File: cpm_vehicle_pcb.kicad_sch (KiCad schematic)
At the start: 71 parts, among them IC1 ATMEGAAU, IC2 RPI-ZERO, J1 Conn_02x03_Counter_Clockwise, J2 Conn_02x03_Counter_Clockwise, J3 Conn_01x05, J5 USB_B_Mini, J6 Conn_01x03_Socket, P1 NCP1117, Q11 BSS123, Q12 BSS123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

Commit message: Some Routing
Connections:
- net ERW1: now also EXT_PINS0.4, IC1.74 ((AD4)PA4); no longer EXT_PINS0.3, IC1.71 ((AD7)PA7)
- net ERW2: now also EXT_PINS0.6, IC1.73 ((AD5)PA5); no longer EXT_PINS0.5, IC1.72 ((AD6)PA6)
- net ERW3: now also EXT_PINS0.8, IC1.72 ((AD6)PA6); no longer EXT_PINS0.7, IC1.73 ((AD5)PA5)
- net ERW4: now also EXT_PINS0.10, IC1.71 ((AD7)PA7); no longer EXT_PINS0.9, IC1.74 ((AD4)PA4)
- net ERW5: now also EXT_PINS0.3; no longer EXT_PINS0.4
- net ERW6: now also EXT_PINS0.5, IC1.7 ((OC3C/INT5)PE5); no longer EXT_PINS0.6, IC1.16 (PH4(OC4B))
- net ERW7: now also EXT_PINS0.7, IC1.6 ((OC3B/INT4)PE4); no longer EXT_PINS0.8, IC1.24 ((OC1A/PCINT5)PB5)
- net ERW8: now also EXT_PINS0.9, IC1.5 ((OC3A/AIN1)PE3); no longer EXT_PINS0.10, IC1.23 ((OC2A/PCINT4)PB4)
- net GND: now also J2.5 (Pin_5); no longer J2.6 (Pin_6)
- net LED1: now also IC1.23 ((OC2A/PCINT4)PB4); no longer IC1.26 ((OC0A/OC1C/PCINT7)PB7)
- net LED2: now also IC1.16 (PH4(OC4B)); no longer IC1.27 (PH7(T4))
- net LED3: now also IC1.17 (PH5(OC4C)); no longer IC1.18 (PH6(OC2B))
- net LED4: now also IC1.18 (PH6(OC2B)); no longer IC1.17 (PH5(OC4C))
- net LED_BUILT_IN: now also IC1.26 ((OC0A/OC1C/PCINT7)PB7); no longer IC1.25 ((OC1B/PCINT6)PB6)
- net PWM: now also IC1.25 ((OC1B/PCINT6)PB6); no longer IC1.8 ((T3/INT6)PE6)
- net RX0: now also IC1.2 ((RXD0/PCIN8)PE0); no longer IC1.4 ((XCK0/AIN0)PE2)
- net SENSOR1: now also J2.6 (Pin_6); no longer J2.3 (Pin_3)
- net SENSOR2: now also J2.4 (Pin_4); no longer J2.5 (Pin_5)
- net SERVO_PWM: now also IC1.24 ((OC1A/PCINT5)PB5); no longer IC1.7 ((OC3C/INT5)PE5)
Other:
- moved on the sheet: C71, QG1

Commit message: update
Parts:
- added J4: USB4105-GF-A, footprints_vehicle_pcb:GCT_USB4105-GF-A, symbol USBC:USB4105-GF-A
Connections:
- net GND: now also J4.A1_B12 (GND), J4.B1_A12 (GND)
- net at C7.2, L1.1, U4.4 (EN)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: now also J4.A4_B9 (VBUS), J4.B4_A9 (VBUS)
- new net: J4.SH1 (SHELL_GND), J4.SH2 (SHELL_GND), J4.SH3 (SHELL_GND), J4.SH4 (SHELL_GND)
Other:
- moved on the sheet: C3, C4, C7, D1, D6, L1, R21, RV1, U4

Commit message: Routing 2
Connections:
- net LED1_PIN: now also J1.5 (Pin_5); no longer J1.3 (Pin_3)
- net LED2_PIN: now also J1.3 (Pin_3); no longer J1.4 (Pin_4)
- net LED4_PIN: now also J1.4 (Pin_4); no longer J1.5 (Pin_5)
- net PWM: now also J3.1 (Pin_1); no longer J3.5 (Pin_5)
- net SERVO_PWM: now also J3.5 (Pin_5); no longer J3.1 (Pin_1)
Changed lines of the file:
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@@
 		)
 	)
-	(label "LED2_PIN"
+	(label "LED4_PIN"
 		(at 66.04 231.14 0)
 		(effects
@@
 		)
 	)
-	(label "SERVO_PWM"
+	(label "PWM"
 		(at 55.88 255.27 0)
 		(effects
@@
 		)
 	)
-	(label "LED1_PIN"
+	(label "LED2_PIN"
 		(at 38.1 231.14 0)
 		(effects
@@
 		)
 	)
-	(label "PWM"
+	(label "SERVO_PWM"
 		(at 59.69 265.43 0)
 		(effects
@@
 		)
 	)
-	(label "LED4_PIN"
+	(label "LED1_PIN"
 		(at 66.04 228.6 0)
 		(effects

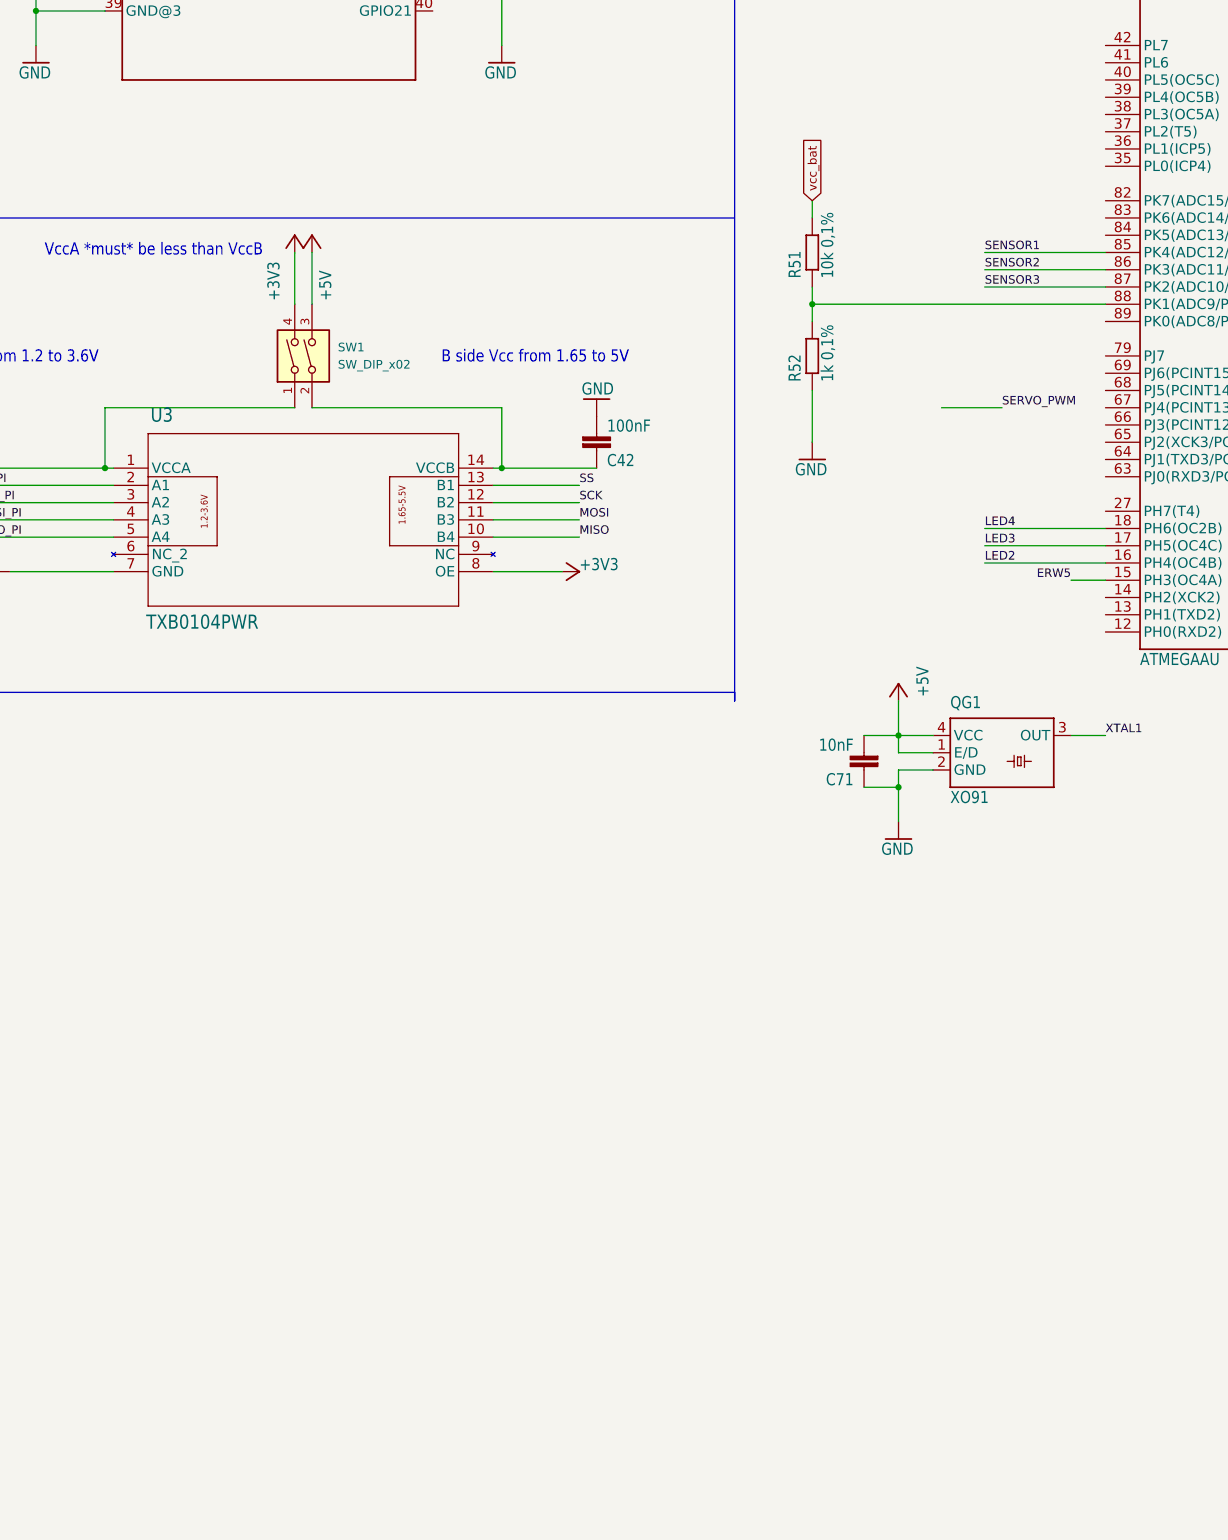
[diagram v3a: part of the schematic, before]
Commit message: Added Bq25887
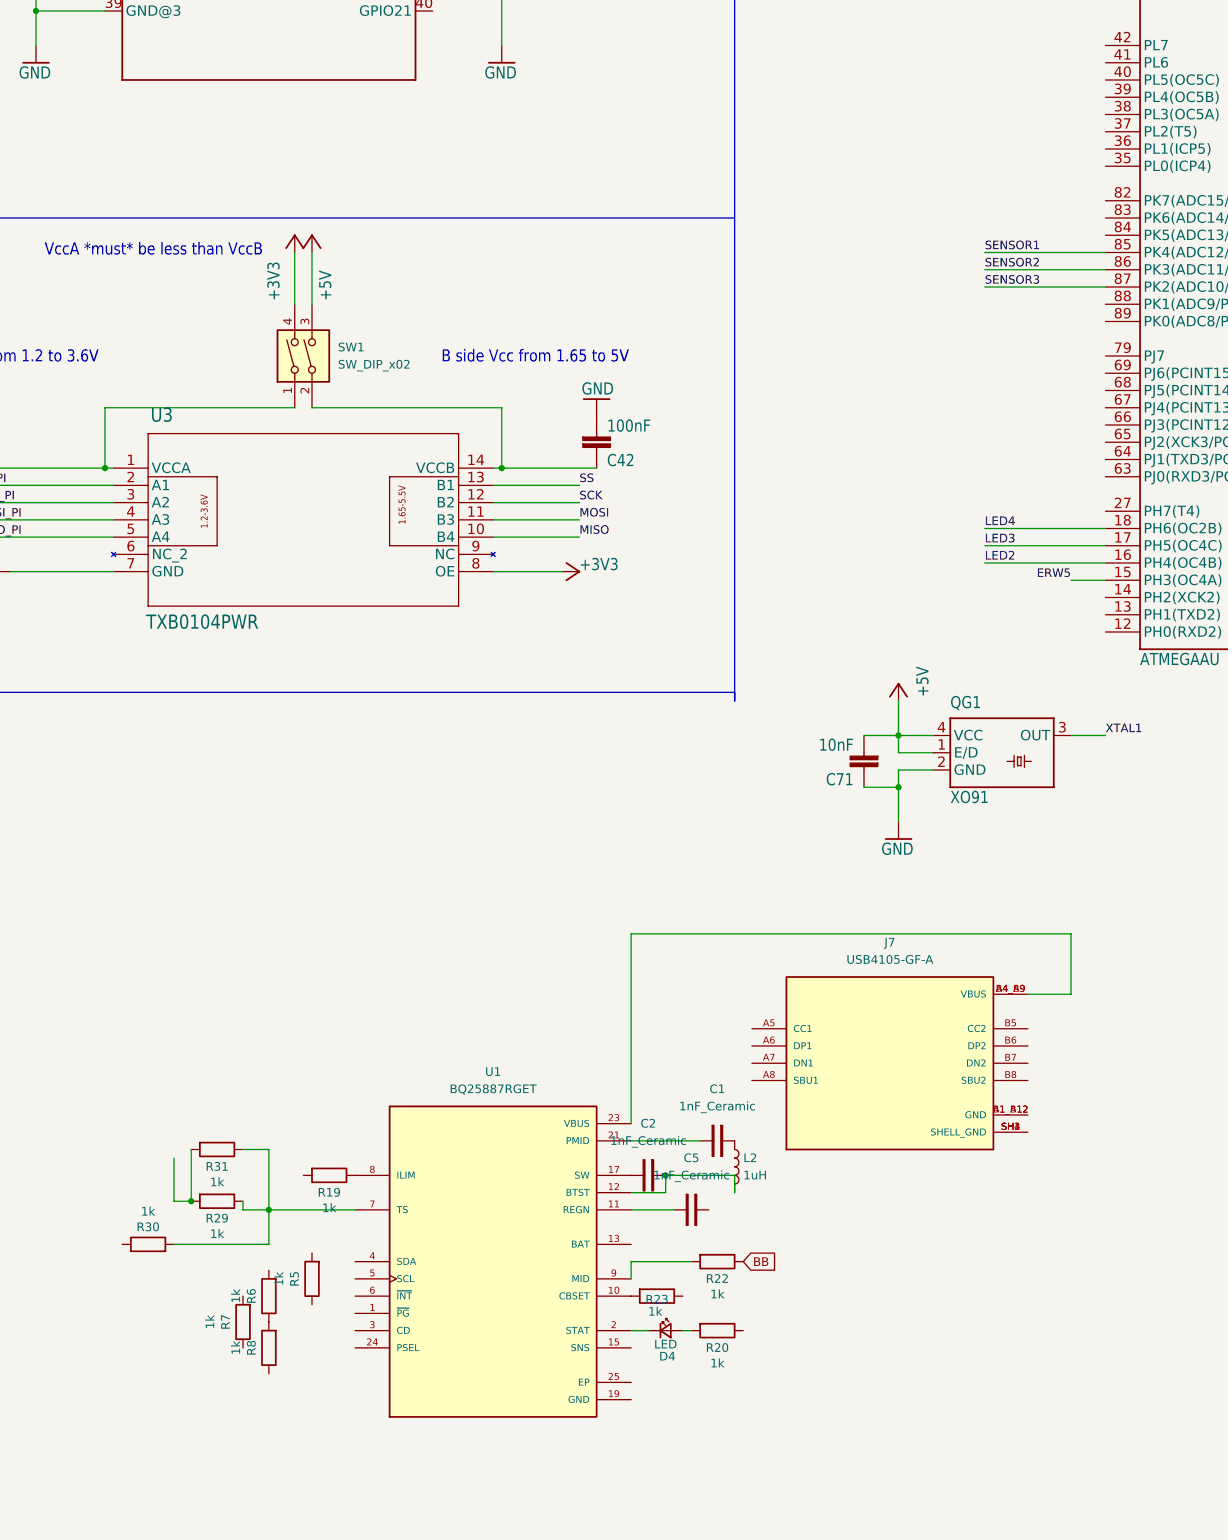
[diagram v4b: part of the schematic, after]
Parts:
- removed R51: 10k 0,1%, Resistor_SMD:R_0603_1608Metric, symbol main_board_V2.4-eagle-import:embedded_10681391_R-EUR0805
- removed R52: 1k 0,1%, Resistor_SMD:R_0603_1608Metric, symbol main_board_V2.4-eagle-import:embedded_10681391_R-EUR0805
- added C1, C2, C5: 1nF_Ceramic, Capacitor_THT:C_Disc_D5.0mm_W2.5mm_P2.50mm, symbol PCM_SL_Capacitors:1nF_Ceramic
- added D4: LED, PCM_SparkFun-LED:LED_0603_1608Metric, symbol PCM_SparkFun-LED:LED
- added J7: USB4105-GF-A, footprints_vehicle_pcb:GCT_USB4105-GF-A, symbol USBC:USB4105-GF-A
- added L2: 1uH, Inductor_SMD:L_10.4x10.4_H4.8, symbol Device:L
- added R19, R20, R22, R23, R29, R30, R31, R5, R6, R7, R8: 1k, Resistor_SMD:R_0603_1608Metric, symbol Device:R
- added U1: BQ25887RGET, BQ25887RGET:QFN50P400X400X100-25N, symbol BQ25887RGET:BQ25887RGET
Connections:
- net BB: now also R22.1
- net GND: now also U1.19 (GND), U1.20 (GND)
- new net: C1.2, L2.1
- new net: D4.1 (K), U1.2 (STAT)
- new net: D4.2 (A), R20.2
- new net: R6.1, R8.2
- new net: R29.1, R30.2, R31.1, U1.7 (TS)
- new net: R29.2, R31.2
- new net: C5.1, U1.11 (REGN)
- new net: R22.2, U1.9 (MID)
- new net: C2.2, L2.2, U1.12 (BTST)
- new net: J7.A1_B12 (GND), J7.B1_A12 (GND)
- new net: J7.A4_B9 (VBUS), J7.B4_A9 (VBUS), U1.23 (VBUS)
- new net: J7.SH1 (SHELL_GND), J7.SH2 (SHELL_GND), J7.SH3 (SHELL_GND), J7.SH4 (SHELL_GND)
- new net: R23.2, U1.10 (CBSET)
- new net: R19.1, U1.8 (ILIM)
- new net: U1.15 (SNS), U1.16 (SNS)
- new net: U1.25 (EP), U1.25_1 (EP), U1.25_2 (EP), U1.25_3 (EP), U1.25_4 (EP), U1.25_5 (EP)
- new net BAT: U1.13 (BAT), U1.14 (BAT)
- new net PMID: C1.1, U1.21 (PMID), U1.22 (PMID)
- new net SW: C2.1, U1.17 (SW), U1.18 (SW)

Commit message: Schematic BQ25887
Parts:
- removed R5, R6, R7, R8: 1k, Resistor_SMD:R_0603_1608Metric, symbol Device:R
- added C12: 10uF, Capacitor_THT:C_Disc_D5.0mm_W2.5mm_P2.50mm, symbol PCM_SL_Capacitors:1nF_Ceramic
- added C6: 1uF, footprints_vehicle_pcb:C0805_10681391, symbol main_board_V2.4-eagle-import:embedded_10681391_C-EUC0805
- added C8: 47nF, Capacitor_THT:C_Disc_D5.0mm_W2.5mm_P2.50mm, symbol PCM_SL_Capacitors:1nF_Ceramic
- C1: value 1nF_Ceramic -> 10uF
- C2: value 1nF_Ceramic -> 44uF
- C5: value 1nF_Ceramic -> 4.7uF
- R19: value 1k -> 383
- R20: value 1k -> 2.2K
- R22: value 1k -> 300
- R29: value 1k -> 5.23K
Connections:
- net B+ is gone; now on net BAT: J6.3 (Pin_3), R25.1, SW2.1 (B)
- net B- is gone; now on net GND: C11.2, C9.2, J6.1 (Pin_1), Q3.3 (S2), U8.6 (VSS)
- net BAT: now also C12.1
- net BB: now also R23.1
- net GND: now also C1.1, C2.2, C5.2, R19.2, R30.1, R31.2, C12.2, C6.2
- net PMID: now also C1.2, L2.1; no longer C1.1
- net SW: now also L2.2, C8.2; no longer C2.1
- net at R30.2, R31.1, U1.7 (TS): now also R29.2; no longer R29.1
- net VREGN: now reaches C5.1, U1.11 (REGN)
- net VREGN: now also R29.1
- net at J7.A4_B9 (VBUS), J7.B4_A9 (VBUS), U1.23 (VBUS): now also C6.1
- net at U1.15 (SNS), U1.16 (SNS): now also C2.1
- new net: C8.1, U1.12 (BTST)
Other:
- moved on the sheet: C1, C5, D4, J7, L2, R20, R22, R23, R29, R30, R31

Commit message: v2
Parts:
- removed C3: 10uF, footprints_vehicle_pcb:C0805_10681391, symbol main_board_V2.4-eagle-import:embedded_10681391_C-EUC0805
- removed C4, C7: 22uF, Capacitor_SMD:C_0603_1608Metric, symbol main_board_V2.4-eagle-import:embedded_10681391_C-EUC0805
- removed D1, D6: SS54, PCM_JLCPCB:D_SMA, symbol PCM_JLCPCB-Diodes:Schottky,SS54
- removed J4: USB4105-GF-A, footprints_vehicle_pcb:GCT_USB4105-GF-A, symbol USBC:USB4105-GF-A
- removed L1: 20uH, Inductor_SMD:L_10.4x10.4_H4.8, symbol Device:L
- removed R21: 3.3K, Resistor_SMD:R_0603_1608Metric, symbol Device:R
- removed RV1: R_Potentiometer, Potentiometer_SMD:Potentiometer_Bourns_3214W_Vertical, symbol Device:R_Potentiometer
- removed U1: BQ25887RGET, BQ25887RGET:QFN50P400X400X100-25N, symbol BQ25887RGET:BQ25887RGET
- removed U4: MT3608, Package_TO_SOT_SMD:SOT-23-6, symbol Regulator_Switching:MT3608
- added U2: BQ25887RGET, BQ25887RGET:QFN50P400X400X100-25N, symbol BQ25887RGET:BQ25887RGET
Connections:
- net BAT: now also U2.13 (BAT), U2.14 (BAT)
- net GND: now also U2.19 (GND), U2.20 (GND)
- net PMID: now also U2.21 (PMID), U2.22 (PMID)
- net SW: now also U2.17 (SW), U2.18 (SW)
- net VREGN: now also U2.11 (REGN)
- net at C2.1: now also U2.15 (SNS), U2.16 (SNS)
- net at D4.1 (K): now also U2.2 (STAT)
- net at R29.2, R30.2, R31.1: now also U2.7 (TS)
- net at R22.2: now also U2.9 (MID)
- net at C6.1, J7.A4_B9 (VBUS), J7.B4_A9 (VBUS): now also U2.23 (VBUS)
- net at C8.1: now also U2.12 (BTST)
- net at R23.2: now also U2.10 (CBSET)
- net at R19.1: now also U2.8 (ILIM)
- new net: U2.25 (EP), U2.25_1 (EP), U2.25_2 (EP), U2.25_3 (EP), U2.25_4 (EP), U2.25_5 (EP)
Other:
- note removed: "Charger"

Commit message: DONE
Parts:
- removed J7: USB4105-GF-A, footprints_vehicle_pcb:GCT_USB4105-GF-A, symbol USBC:USB4105-GF-A
- added J4: USB3090-XX-X_REVE2, USB3090-XX-X_REVE2:GCT_USB3090-XX-X_REVE2, symbol USB3090-XX-X_REVE2:USB3090-XX-X_REVE2
- added R5, R6: 1k, Resistor_SMD:R_0603_1608Metric, symbol Device:R
- C1, C12, C2, C5, C8: footprint Capacitor_THT:C_Disc_D5.0mm_W2.5mm_P2.50mm -> footprints_vehicle_pcb:C0805_10681391
- D4: footprint PCM_SparkFun-LED:LED_0603_1608Metric -> LED_SMD:LED_0805_2012Metric
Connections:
- net +5V: now also R20.1, R5.2, R6.1
- net +8.5V: now also C12.1, U2.13 (BAT), U2.14 (BAT)
- net GND: now also J4.5 (GND), J4.SH1 (SHIELD), J4.SH2 (SHIELD), J4.SH3 (SHIELD), J4.SH4 (SHIELD); no longer C11.2, C9.2, J6.1 (Pin_1), Q3.3 (S2), U8.6 (VSS)
- net SCL: now also U2.5 (SCL), R5.1
- net SDA: now also U2.4 (SDA), R6.2
- net SDA1: now reaches IC2.3 (GPIO2/SDA1)
- net SCL1: now reaches IC2.5 (GPIO3/SCL1)
- net at C6.1, U2.23 (VBUS): now also J4.1 (VBUS)
- net BAT renamed B+
- net B+: no longer C12.1, U2.13 (BAT), U2.14 (BAT)
- new net B-: C11.2, C9.2, J6.1 (Pin_1), Q3.3 (S2), U8.6 (VSS)
- no-connect marks 0 -> 101
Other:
- moved on the sheet: C1, C12, C2, C5, C6, C8, D4, L2, R/W0, R19, R20, R22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

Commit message: some changes
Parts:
- removed SW1: SW_DIP_x02, Button_Switch_SMD:SW_DIP_SPSTx02_Slide_9.78x7.26mm_W8.61mm_P2.54mm, symbol Switch:SW_DIP_x02
- removed SW2: SW_SPDT_312, Button_Switch_THT:SW_Slide-03_Wuerth-WS-SLTV_10x2.5x6.4_P2.54mm, symbol Switch:SW_SPDT_312
- added R21: 20k, symbol Device:R
- added R7: 10k, Resistor_SMD:R_0603_1608Metric, symbol Device:R
- added R8: 47k, symbol Device:R
- added SW1: SW_DIP_x01, symbol Switch:SW_DIP_x01
- added SW2: SW_SPST, symbol Switch:SW_SPST
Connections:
- net B+ is gone; now on net +8.5V: J6.3 (Pin_3), R25.1
- net +3V3: now also C41.1, U3.1 (VCCA), SW1.2; no longer U3.8 (OE)
- net +5V: now also C42.1, U3.14 (VCCB); no longer R20.1
- net +8.5V: now also SW2.1 (A)
- net GND: now also R21.2, R8.2
- net vcc_bat: now also R8.1, SW2.2 (B)
- net VBUS: now reaches C6.1, J4.1 (VBUS), U2.23 (VBUS)
- net VBUS: now also R20.1, R7.1
- net at U2.24 (PSEL): now also R7.2
- new net: R21.1, SW1.1, U3.8 (OE)
- no-connect marks 101 -> 100
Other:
- note added: "Atmega 2560 (LLC)"
- note added: "Battery charging and monitoring system"
- note added: "Extension Pins"
- note added: "Identification LEDs"
- note added: "Level Shifter"
- note added: "RPi Zero (MLC)"
- note added: "Sensors"
- note added: "Servo and ESC"
- note added: "USB to Serial"
- note added: "Voltage Regulator (Battery -> 5V)"
- note removed: "Battery monitoring system"
- moved on the sheet: A1, C1, C10, C12, C2, C41, C42, C5, C51, C53, C54, C55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
